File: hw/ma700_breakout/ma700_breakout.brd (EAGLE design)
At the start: 35 x 15 mm, 3 parts

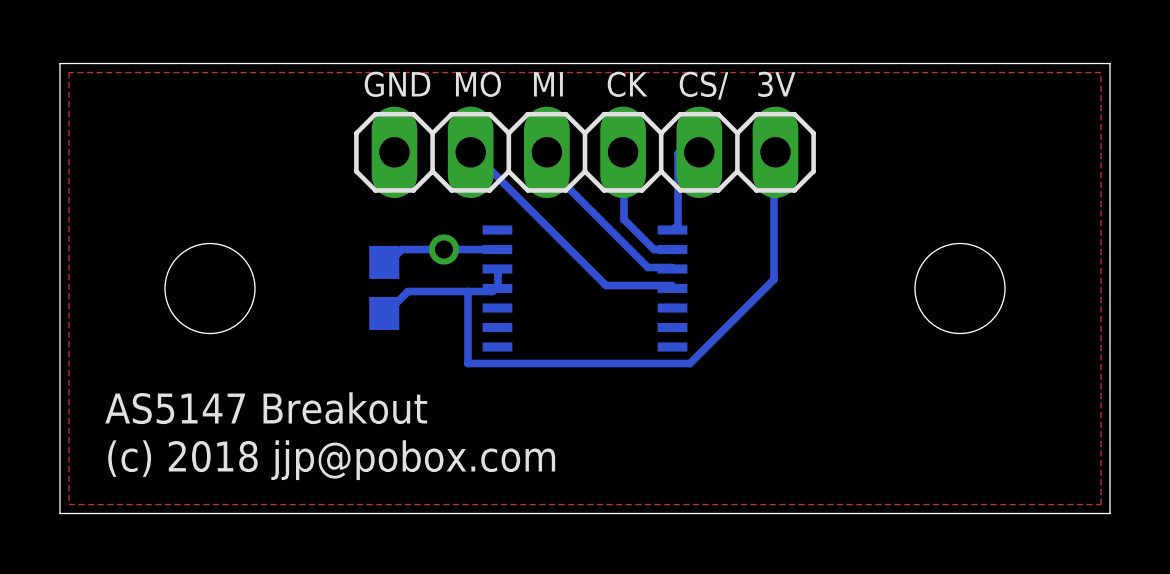
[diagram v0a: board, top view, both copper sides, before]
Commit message: Rename AS5147->AS5047 which actually seems to exist
Add a MA700 breakout, which I may or may not need
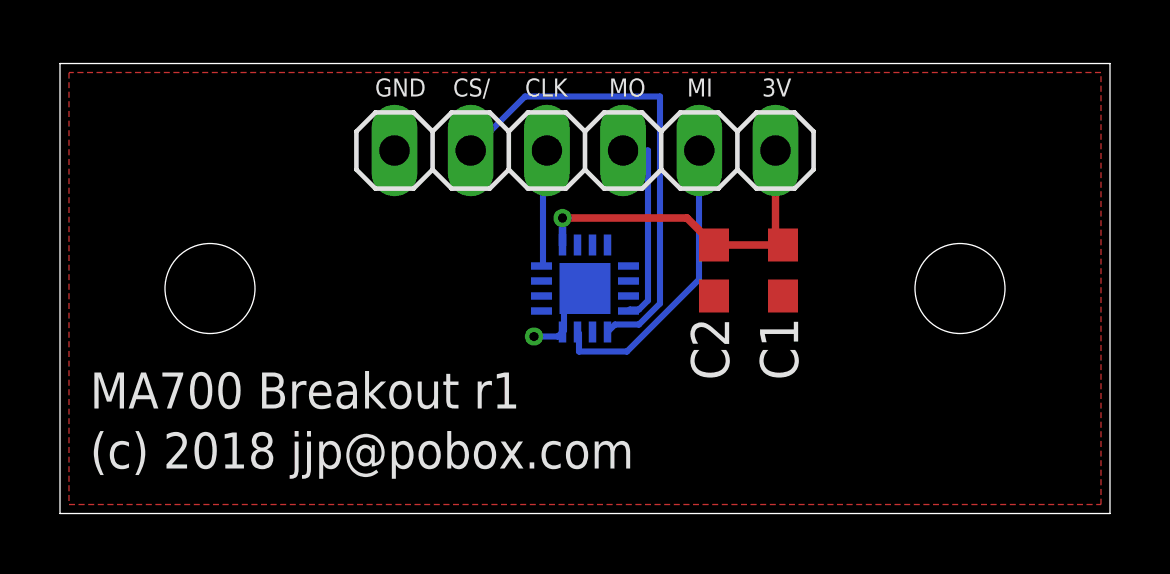
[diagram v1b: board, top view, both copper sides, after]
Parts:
- removed U$1: AS5147, as5147_breakout:TSSOP14
- added C2: .1uF, rcl:C0603
- added U1: MA700, ma700_breakout:QFN-16
- C1: value 0.1uF -> 1uF
- moved C1 13.3 mm to (24.1, 8.10), flipped to the top, turned to 270 degrees
- moved JP1 0.06 mm to (17.5, 12.1), turned to 0 degrees
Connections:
- removed net N$6: JP1.2, U$1.1
- new net N$2: JP1.2, U1.5
- net GND: now also C2.2, JP1.1, U1.8, U1.PAD; no longer JP1.6, U$1.13
- net N$3: now also JP1.3, U1.12; no longer JP1.5, U$1.4
- net N$4: now also U1.4; no longer U$1.3
- net N$5: now also JP1.5, U1.7; no longer JP1.3, U$1.2
- net VCC: now also C2.1, JP1.6, U1.13; no longer JP1.1, U$1.11, U$1.12
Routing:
- net N$2: track 0.00 -> 16.1 mm
- net VCC: track 22.8 -> 11.9 mm, vias 0 -> 1
- net N$5: track 4.28 -> 9.97 mm
- net N$3: track 8.64 -> 4.00 mm
- net N$6: track 3.35 -> 0.00 mm
- net GND: track 3.94 -> 3.18 mm
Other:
- board text added: "CLK"
- board text added: "MA700 Breakout r1"
- board text removed: "AS5147 Breakout"
- board text removed: "CK"
